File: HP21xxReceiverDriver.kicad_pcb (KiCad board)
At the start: 2 copper layers, 34.8 x 57.6 mm, 102 parts, among them J1 DIP24, J2 DIP24, J3 DIP24, Q1 MMBT2369A, Q10 MMBT2369A, Q11 MMBT2369A, Q12 MMBT2369A, Q13 MMBT2369A, Q14 MMBT2369A, Q15 MMBT2369A, Q16 MMBT2369A, Q17 MMBT2369A, Q18 MMBT2369A, Q2 MMBT2369A, Q3 MMBT2369A, Q4 MMBT2369A, Q5 MMBT2369A, Q6 MMBT2369A, Q7 MMBT2369A, Q8 MMBT2369A, Q9 MMBT2369A, U1 74ACT04, U2 AMS1117-3.3, U4 AMS1117-3.3

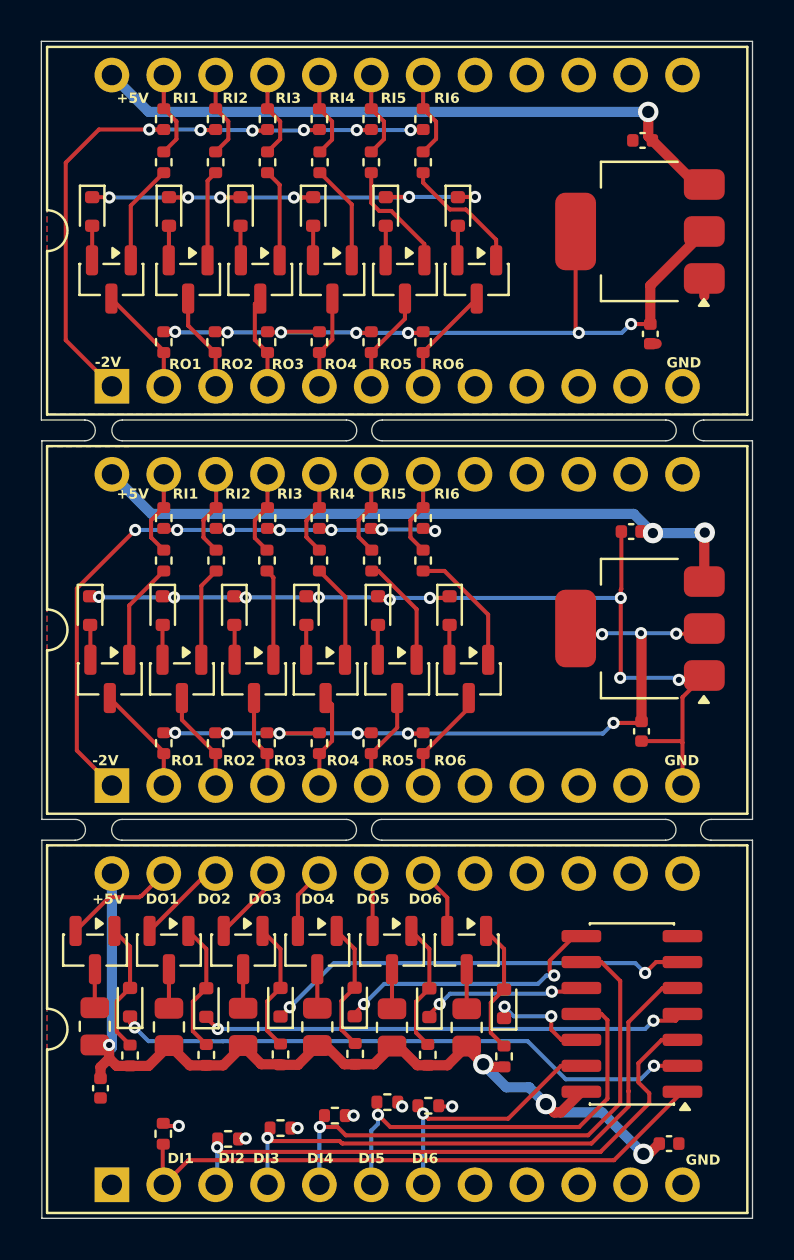
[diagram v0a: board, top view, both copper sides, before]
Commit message: Updated schematics and pcb for 3.3V pullups on the driver inputs.
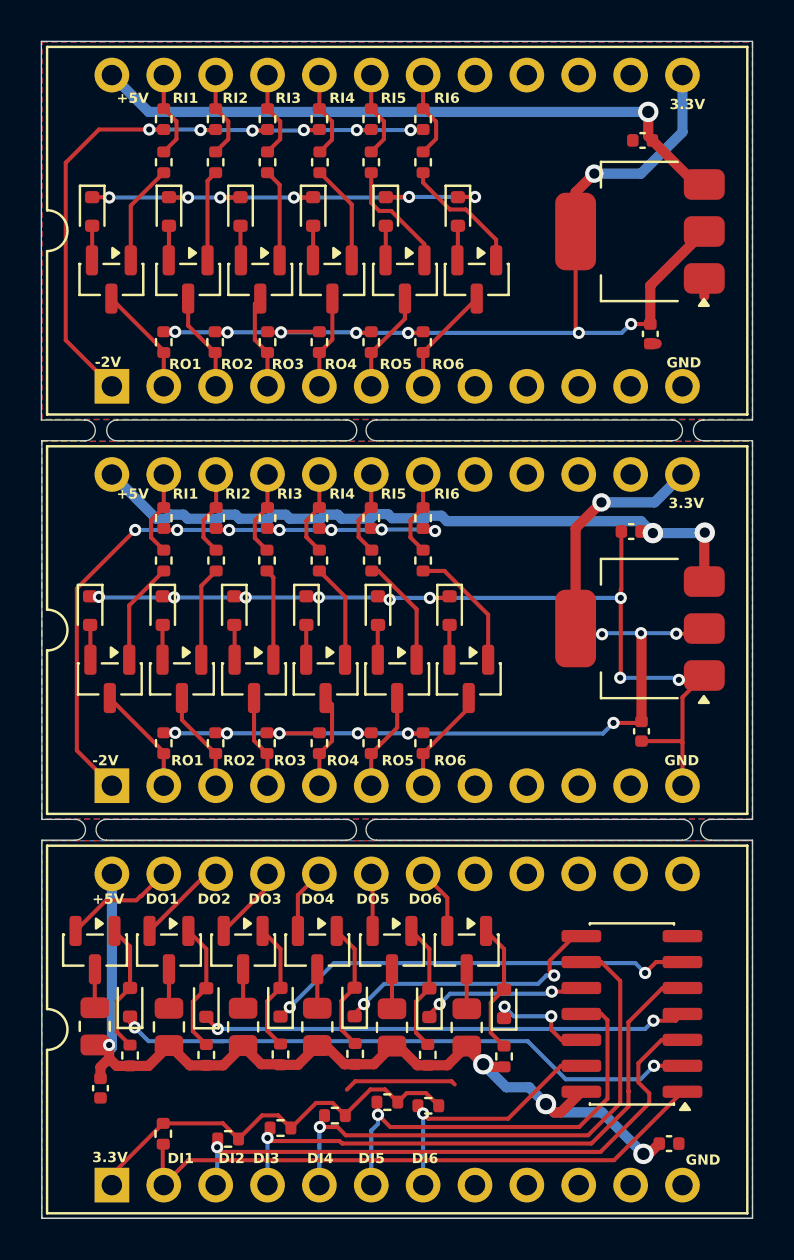
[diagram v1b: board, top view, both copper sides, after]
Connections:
- J1 pad 1: unconnected-(J1-Pin_1-Pad1) -> /PLUS3_3V_IN
- J2 pad 13: unconnected-(J2-Pin_13-Pad13) -> /PLUS3V3R2
- J3 pad 13: unconnected-(J3-Pin_13-Pad13) -> /PLUS3V3R1
- R49 pad 1: /PLUS5D -> /PLUS3_3V_IN
- R50 pad 1: /PLUS5D -> /PLUS3_3V_IN
- R51 pad 1: /PLUS5D -> /PLUS3_3V_IN
- R52 pad 1: /PLUS5D -> /PLUS3_3V_IN
- R53 pad 1: /PLUS5D -> /PLUS3_3V_IN
- R54 pad 1: /PLUS5D -> /PLUS3_3V_IN
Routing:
- net /PLUS3_3V_IN: track 0.00 -> 21.0 mm
- net /PLUS3V3R2: track 39.1 -> 50.4 mm, vias 9 -> 10
- net /PLUS3V3R1: track 39.4 -> 50.6 mm, vias 7 -> 8
- net /GNDD: track 0.00 -> 5.52 mm
- net /PLUS5D: track 50.8 -> 47.9 mm, vias 10 -> 4
- net /PLUS5VR2: track 33.3 -> 34.2 mm
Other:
- outline, holes or cut-outs redrawn
- board text added: "3.3V"
